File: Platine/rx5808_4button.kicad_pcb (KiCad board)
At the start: 2 copper layers, 50 x 29.5 mm, 52 parts, among them IC1 ATMEGA328-A, P1 CONN_01X04, P2 CONN_01X05, P6 CONN_01X04, P7 CONN_02X05, U1 TPS62160, U2 RX5808, U3 sn74lvc1g3157, U4 MCPL3-BC-V, Y1 16 MHz

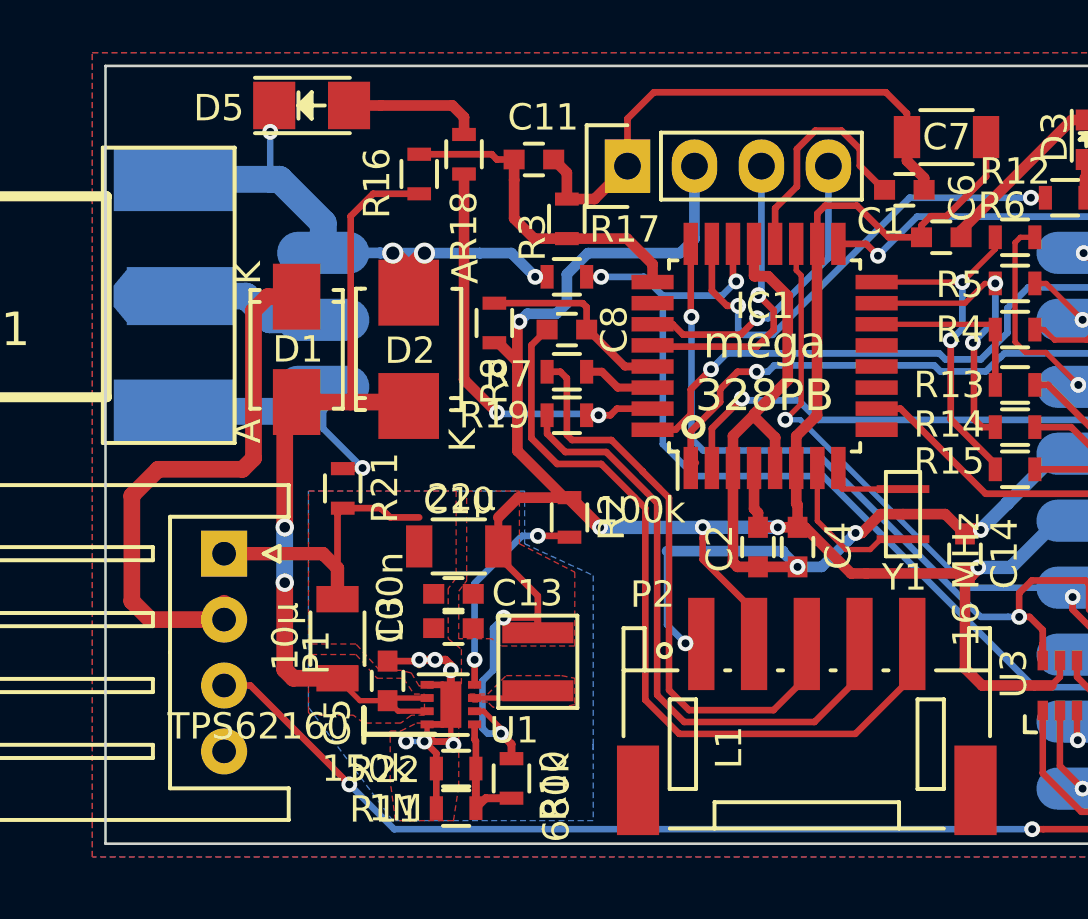
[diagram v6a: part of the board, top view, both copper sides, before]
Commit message: RC-Filter für OLED hinzugefügt und eingelayoutet
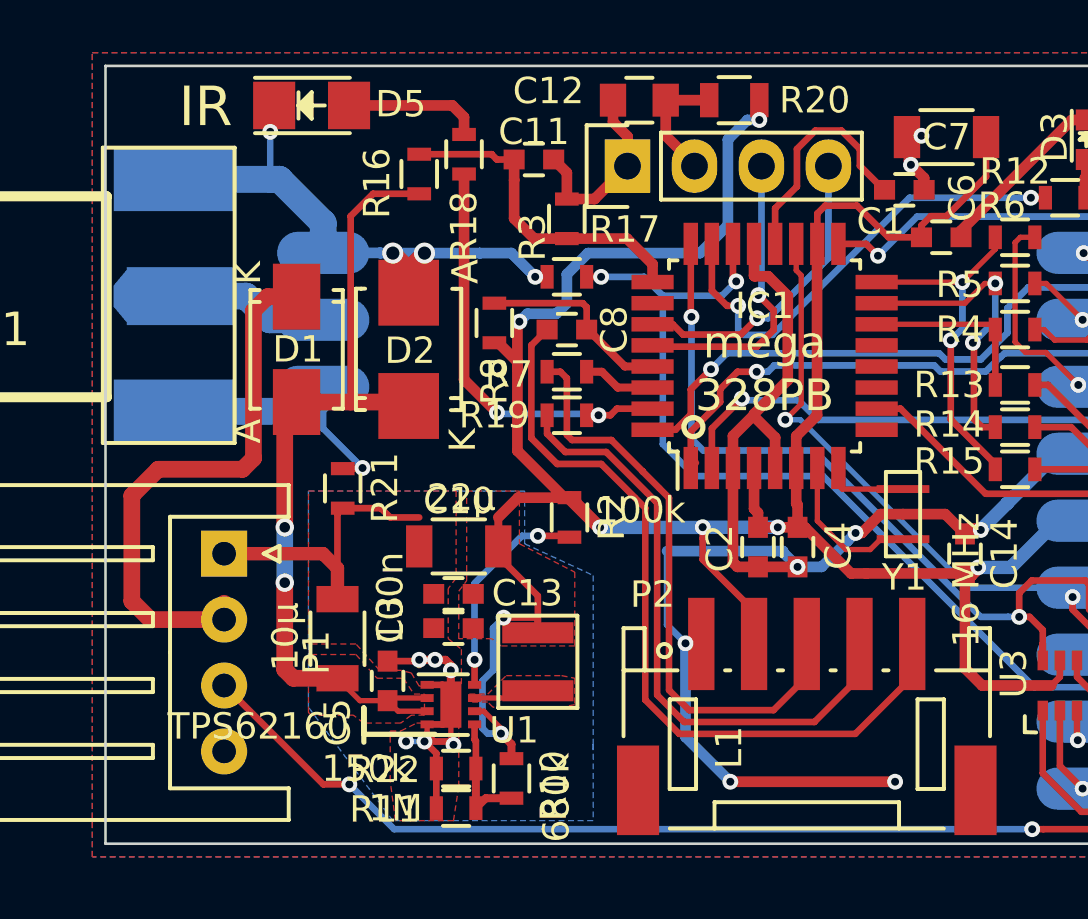
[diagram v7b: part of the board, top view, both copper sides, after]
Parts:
- added C12: 4,7u, Capacitors_SMD:C_0805, F.Cu at (133.2, 96.3)
- added R20: 10, Resistors_SMD:R_0805, F.Cu at (136.8, 96.3)
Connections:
- P6 pad 2: +5V -> Net-(C12-Pad1)
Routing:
- net Net-(C12-Pad1): track 0.00 -> 5.64 mm
- net +5V: track 113.4 -> 116.5 mm, vias 7 -> 8
- net GND: track 132.5 -> 133.9 mm, vias 11 -> 15
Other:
- board text added: "IR"

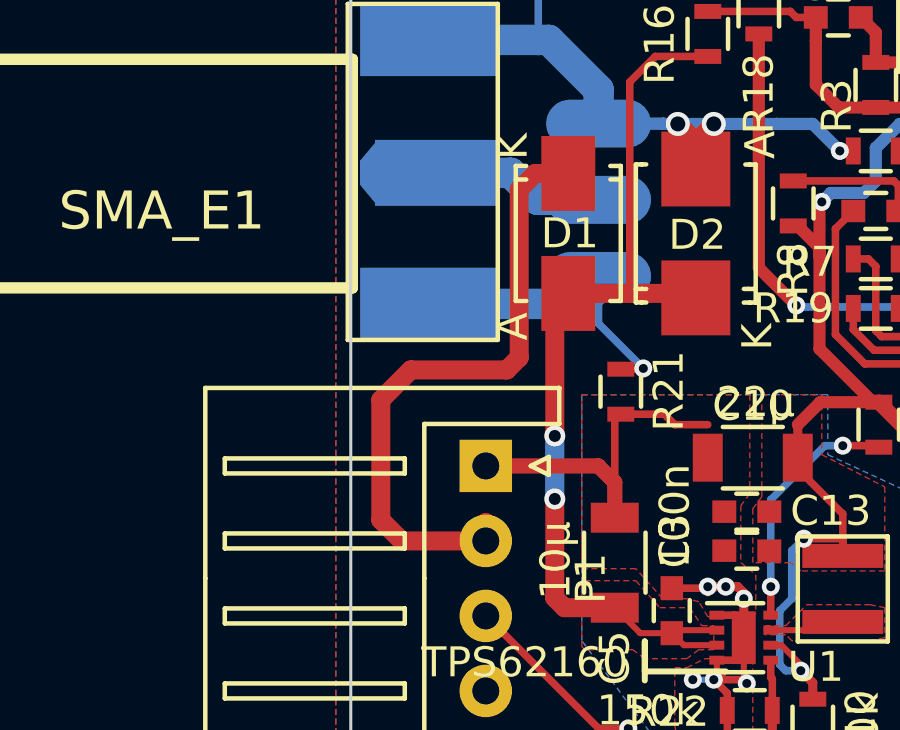
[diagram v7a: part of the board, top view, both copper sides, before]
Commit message: BOM hinzugefügt
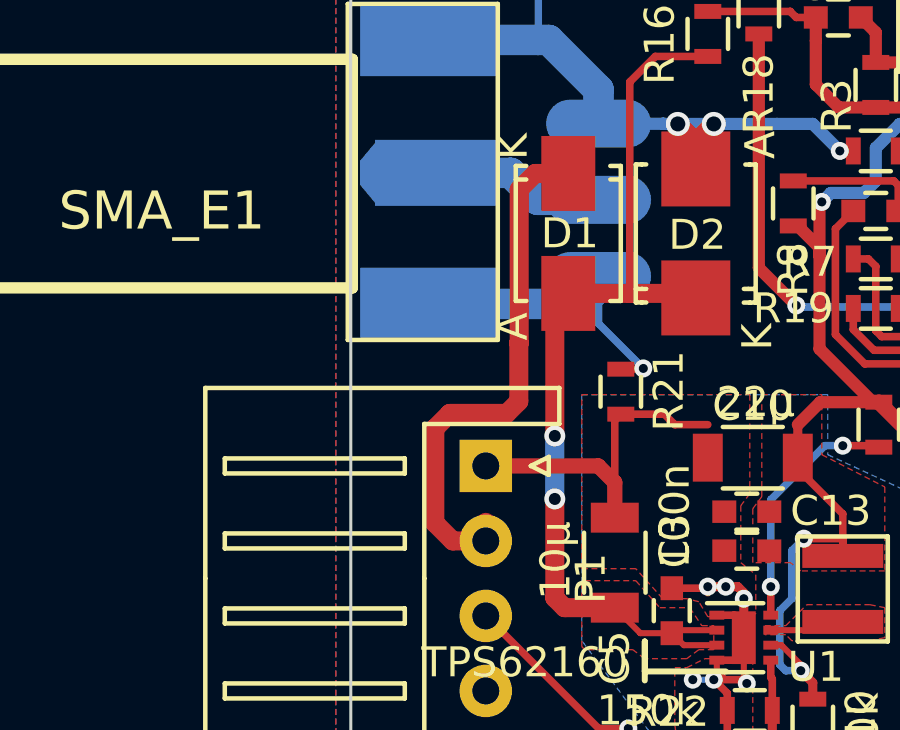
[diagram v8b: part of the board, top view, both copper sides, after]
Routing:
- net Net-(D1-Pad1): track 21.1 -> 17.8 mm
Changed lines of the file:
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@@
-(kicad_pcb (version 4) (host pcbnew "(2016-05-25 BZR 6829)-product")
+(kicad_pcb (version 4) (host pcbnew "(2016-08-12 BZR 7023)-product")
   (general
     (links 128)
     (no_connects 0)
-    (area 112.949999 94.949999 163.050001 124.550001)
+    (area 99.959499 90.3 177.400001 126.7925)
     (thickness 1.6)
     (drawings 14)
-    (tracks 679)
+    (tracks 681)
     (zones 0)
     (modules 54)
@@
   )
   (layers
-    (0 F.Cu signal hide)
-    (31 B.Cu signal hide)
+    (0 F.Cu signal)
+    (31 B.Cu signal)
+    (34 B.Paste user)
+    (35 F.Paste user)
     (36 B.SilkS user)
     (37 F.SilkS user)
@@
   )
   (setup
-    (last_trace_width 0.4064)
+    (last_trace_width 0.25)
     (user_trace_width 0.2032)
     (user_trace_width 0.254)
@@
     (mod_text_size 1 1)
     (mod_text_width 0.15)
-    (pad_size 4.07162 1.99898)
+    (pad_size 1.6 3.4)
     (pad_drill 0)
     (pad_to_mask_clearance 0.1)
@@
     (visible_elements FFFEEF39)
     (pcbplotparams
-      (layerselection 0x010f0_ffffffff)
-      (usegerberextensions true)
-      (excludeedgelayer true)
+      (layerselection 0x00080_7ffffffe)
+      (usegerberextensions false)
+      (excludeedgelayer false)
       (linewidth 0.100000)
       (plotframeref false)
@@
       (plotinvisibletext false)
       (padsonsilk false)
-      (subtractmaskfromsilk true)
-      (outputformat 1)
+      (subtractmaskfromsilk false)
+      (outputformat 5)
       (mirror false)
       (drillshape 0)
@@
     (pad 5 smd rect (at 4 -2.775) (size 1 3.5) (layers F.Cu F.Mask)
       (net 6 /DTR))
-    (pad "" smd rect (at -6.4 2.775) (size 1.6 3.4) (layers F.Cu F.Mask))
-    (pad "" smd rect (at 6.4 2.775) (size 1.6 3.4) (layers F.Cu F.Mask))
+    (pad "" smd rect (at -6.4 2.775) (size 1.6 3.4) (layers F.Cu F.Mask)
+      (zone_connect 2))
+    (pad "" smd rect (at 6.4 2.775) (size 1.6 3.4) (layers F.Cu F.Mask)
+      (zone_connect 2))
   )
   (module Resistors_SMD:R_0805 (layer F.Cu)
@@
   (segment (start 133.075316 111.368612) (end 131.804571 110.097867) (width 0.254) (layer F.Cu) (net 6))
   (segment (start 129.154165 105.595835) (end 129.75 105) (width 0.254) (layer F.Cu) (net 6) (status 20))
+  (segment (start 117.5 116) (end 116.4 116) (width 0.635) (layer F.Cu) (net 7))
+  (segment (start 118.6 109.4) (end 118.613627 109.4) (width 0.635) (layer F.Cu) (net 7))
+  (segment (start 118.6 111.35) (end 118.6 109.4) (width 0.635) (layer F.Cu) (net 7))
+  (segment (start 118.2 111.75) (end 118.6 111.35) (width 0.635) (layer F.Cu) (net 7))
+  (segment (start 116.3 111.75) (end 118.2 111.75) (width 0.635) (layer F.Cu) (net 7))
+  (segment (start 115.8 112.25) (end 116.3 111.75) (width 0.635) (layer F.Cu) (net 7))
+  (segment (start 115.8 115.4) (end 115.8 112.25) (width 0.635) (layer F.Cu) (net 7))
+  (segment (start 116.4 116) (end 115.8 115.4) (width 0.635) (layer F.Cu) (net 7))
   (segment (start 120.25 103.75102) (end 119.14898 103.75102) (width 0.635) (layer F.Cu) (net 7) (status 10))
+  (segment (start 118.613627 104.286373) (end 118.613627 109.4) (width 0.635) (layer F.Cu) (net 7))
   (segment (start 119.14898 103.75102) (end 118.613627 104.286373) (width 0.635) (layer F.Cu) (net 7))
-  (segment (start 118.2 110.3) (end 115 110.3) (width 0.635) (layer F.Cu) (net 7))
-  (segment (start 118.613627 104.286373) (end 118.613627 109.886373) (width 0.635) (layer F.Cu) (net 7))
-  (segment (start 118.613627 109.886373) (end 118.2 110.3) (width 0.635) (layer F.Cu) (net 7))
-  (segment (start 114 115.3) (end 114.7 116) (width 0.635) (layer F.Cu) (net 7))
-  (segment (start 114.7 116) (end 117.5 116) (width 0.635) (layer F.Cu) (net 7) (status 20))
-  (segment (start 115 110.3) (end 114 111.3) (width 0.635) (layer F.Cu) (net 7))
-  (segment (start 114 111.3) (end 114 115.3) (width 0.635) (layer F.Cu) (net 7))
   (segment (start 117.5 116) (end 117.5 115.380547) (width 0.635) (layer F.Cu) (net 7) (status 30))
   (segment (start 150.15 100) (end 150.15 99.25) (width 0.4064) (layer F.Cu) (net 8) (status 10))
@@
         (xy 128.7 113.125) (xy 130.8 114.2) (xy 130.8 117) (xy 128 117) (xy 127.65625 116.725)
         (xy 126.4 116.725) (xy 126.4 114.925) (xy 126.7 114.525) (xy 126.7 111.125) (xy 128.7 111.125)
-        (xy 128.7 113.125)
       )
     )
